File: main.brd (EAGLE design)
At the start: 49.5 x 51.7 mm, 37 parts, among them J1 CORTEX_DEBUG_PTH, U1 ATSAMD21G-A, U2 BNO055, U3 BQ24133_RGY_24

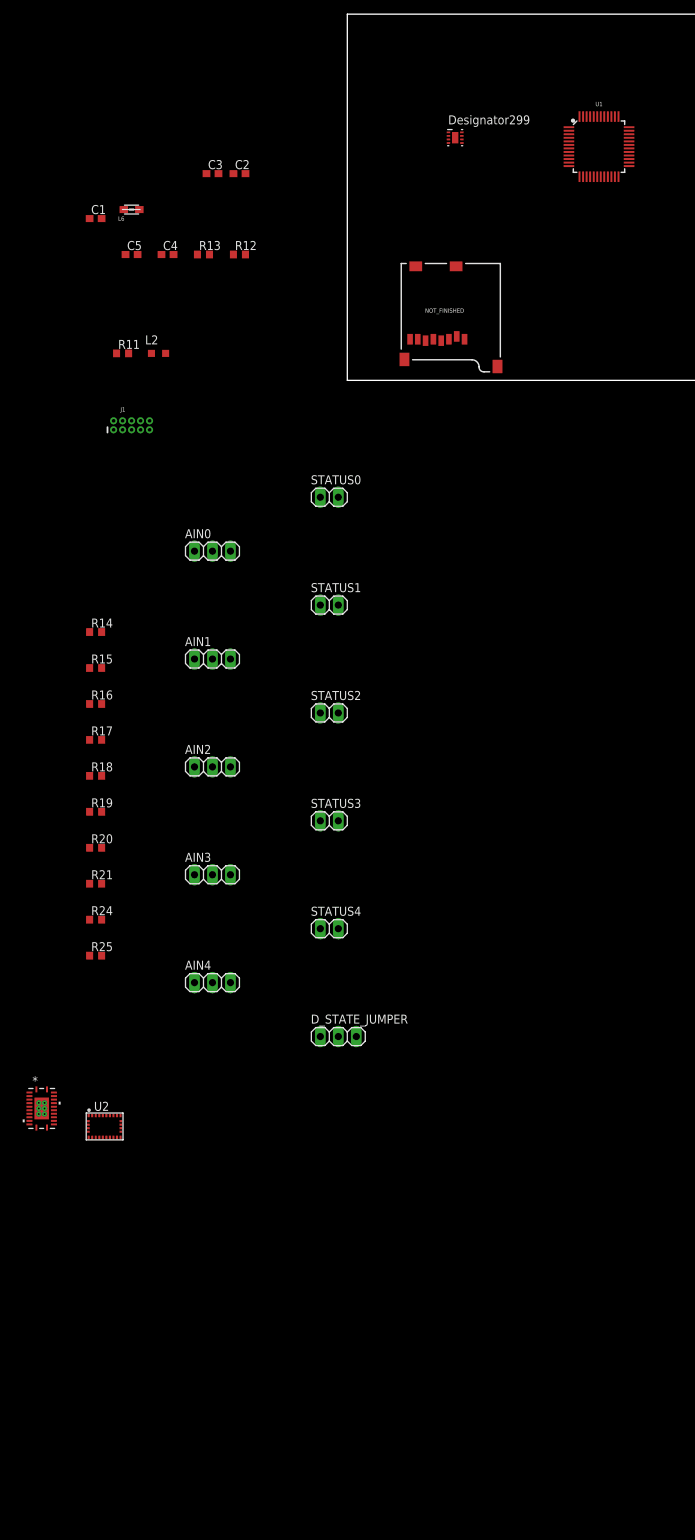
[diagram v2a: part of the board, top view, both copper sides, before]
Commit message: Added IMU Configuration
Added Imu Nets
Removed AIO and GPIO Net assignments for now, since they can go anywhere
Named SD CARD SPI pins accordingly, these should be final
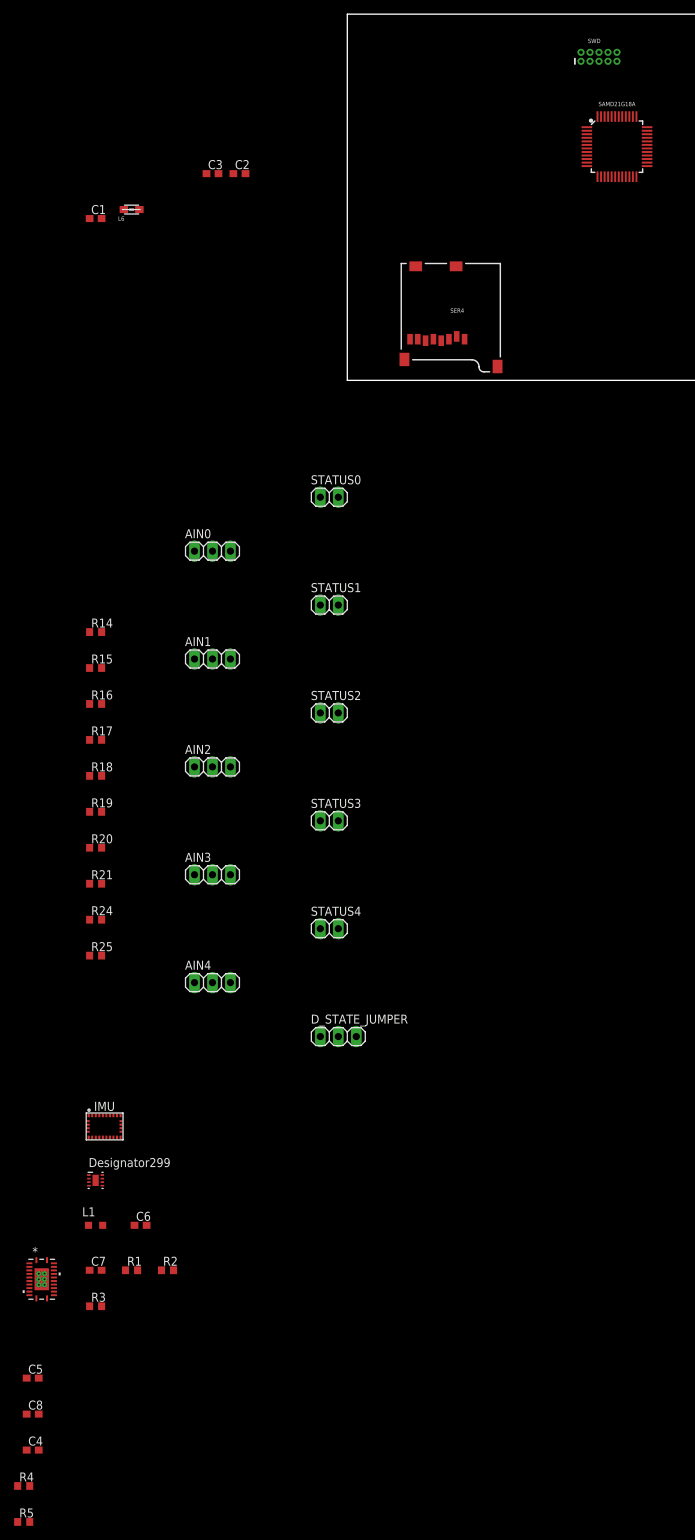
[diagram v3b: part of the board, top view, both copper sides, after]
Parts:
- removed J1: CORTEX_DEBUG_PTH, SparkFun-Connectors:2X5-PTH-1.27MM
- removed L2: REF, resistor:L2012C
- removed PWR_REG: (no value), TPS62162-Q1:DSG0008A
- removed R11, R12, R13: REF, resistor:R0603
- removed U1: ATSAMD21G-A, SparkFun-IC-Microcontroller:TQFP-48
- removed U3: BQ24133_RGY_24, BQ24133:RGY24_2P05X3P1
- added 3.3V_REG: (no value), TPS62162-Q1:DSG0008A
- added C6, C7: REF, resistor:C0603
- added C8: 100nF, resistor:C0603
- added L1: REF, resistor:L2012C
- added POWER_CONTROLLER: BQ24133_RGY_24, BQ24133:RGY24_2P05X3P1
- added R1, R2, R3: REF, resistor:R0603
- added R4, R5: 10k, resistor:R0603
- added SAMD21G18A: ATSAMD21G-A, SparkFun-IC-Microcontroller:TQFP-48
- added SWD: CORTEX_DEBUG_PTH, SparkFun-Connectors:2X5-PTH-1.27MM
- C3: value 0.1uF -> 100nF
- C4: value REF -> 6.8nF
- C5: value REF -> 100nF
- moved C4 170.0 mm to (-44.5, -151.1)
- moved C5 159.4 mm to (-44.5, -141.0)
- renumbered NOT_FINISHED to SER4, U2 to IMU
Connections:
- removed net GNDIO: IMU.25
- removed net N$6: L2.1, PWR_REG.7
- removed net PIN10: IMU.10
- removed net PIN15: IMU.15
- removed net PIN16: IMU.16
- removed net SPI_DEFAULT_SS: U1.27
- removed net SPI_MISO: SER4.DO, U1.28
- removed net SPI_MOSI: SER4.DI, U1.25
- removed net SPI_SCK: SER4.SCLK, U1.26
- removed net VDD: IMU.3
- removed net VDDIO: IMU.28
- removed net ~RESET: J1.10, U1.40
- removed net ~SD_CS: SER4.CS
- new net *I2C_ADDR_SEL: IMU.17
- new net *I2C_SCL: IMU.19
- new net *I2C_SDA: IMU.20
- new net *INT: IMU.14
- new net *NBL_IMU: IMU.4
- new net *XIN32: IMU.27
- new net *XOUT32: IMU.26
- new net N$10: 3.3V_REG.5, R1.1, R2.2
- new net N$7: 3.3V_REG.7, L1.1
- new net NRESET: IMU.11, R4.2, R5.2, SAMD21G18A.40, SWD.10
- new net PA14_PORT: SAMD21G18A.23, SER4.CD1, SER4.CD2
- new net PA15_PORT: SAMD21G18A.24, SER4.CS
- new net PB08D_SER4_P0: SAMD21G18A.7, SER4.DI
- new net PB09D_SER4_P1: SAMD21G18A.8, SER4.SCLK
- new net PB11D_SER4_P3: SAMD21G18A.20, SER4.DO
- net 3.3V: now also 3.3V_REG.6, C4.1, C6.1, IMU.28, IMU.3, L1.2, R1.2, R3.2, R4.1, R5.1, SAMD21G18A.44, SWD.1; no longer J1.1, L2.2, PWR_REG.6, R11.2, R12.2, U1.44
- net AVCC: now also POWER_CONTROLLER.4; no longer U3.4
- net BTST: now also POWER_CONTROLLER.21; no longer U3.21
- net EPAD: now also POWER_CONTROLLER.25; no longer U3.25
- net GND: now also 3.3V_REG.1, 3.3V_REG.4, 3.3V_REG.9, C6.2, C7.2, C8.2, IMU.10, IMU.15, IMU.16, IMU.18, IMU.25, IMU.5, IMU.6, R2.1, SAMD21G18A.18, SAMD21G18A.35, SAMD21G18A.42, SAMD21G18A.5, SWD.3, SWD.5, SWD.9; no longer J1.3, J1.5, J1.9, PWR_REG.1, PWR_REG.4, PWR_REG.9, R13.1, U1.18, U1.35, U1.42, U1.5
- net N$2: now also SAMD21G18A.6; no longer U1.6
- net N$9: now also C8.1, IMU.9; no longer PWR_REG.5, R12.1, R13.2
- net PA02_AIN0: no longer U1.3
- net PA04_AIN4: no longer U1.9
- net PA05_AIN5: no longer U1.10
- net PA30_SWCLK: now also SAMD21G18A.45, SWD.4; no longer J1.4, U1.45
- net PA31_SWDIO: now also SAMD21G18A.46, SWD.2; no longer J1.2, U1.46
- net PB08_AIN2: no longer U1.7
- net PB09_AIN3: no longer U1.8
- net PG: now also 3.3V_REG.8, R3.1; no longer PWR_REG.8, R11.1
- net PGND: now also POWER_CONTROLLER.23; no longer U3.23
- net PGND_2: now also POWER_CONTROLLER.22; no longer U3.22
- net PVCC: now also POWER_CONTROLLER.3; no longer U3.3
- net PVCC_2: now also POWER_CONTROLLER.2; no longer U3.2
- net REGN: now also POWER_CONTROLLER.20; no longer U3.20
- net SW: now also POWER_CONTROLLER.24; no longer U3.24
- net SW_2: now also POWER_CONTROLLER.1; no longer U3.1
- net VDDCORE: now also SAMD21G18A.43; no longer U1.43
- net VIN: now also 3.3V_REG.2, 3.3V_REG.3, C7.1; no longer C4.1, PWR_REG.2, PWR_REG.3
- net VREF: now also POWER_CONTROLLER.12; no longer U3.12

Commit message: Added lib folder, added charge controller schematic
Almost finished naming nets and component values.
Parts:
- removed STATUS0, STATUS1, STATUS2, STATUS3, STATUS4: (no value), pinhead:1X02
- added BATT, V0, V1, V2: (no value), pinhead:1X02
- added C11, C21, C23: 1u, resistor:C0603
- added C12: 2.2u, resistor:C0603
- added C13, C14, C16, C18, C22: 100n, resistor:C0603
- added C15, C19, C20: 10u, resistor:C0603
- added C17: 47n, resistor:C0603
- added C9: 100nF, resistor:C0603
- added D1: BAS70-05, diode:SOT23
- added L2: 3.3u, resistor:L2012C
- added LED1: (no value), adafruit:CHIPLED_0603
- added Q1, Q2: 5.8A/30V/35mΩ, SparkFun-DiscreteSemi:SOT23-3
- added Q3: 2.5A/30V/105mΩ, SparkFun-DiscreteSemi:SOT23-3
- added R10: 2, resistor:R0603
- added R11, R12: 4.02k, resistor:R0603
- added R13: 20m, resistor:R0603
- added R23, R33: 0, resistor:R0603
- added R26: 1k, resistor:R0603
- added R27: 10m, resistor:R0603
- added R28: 232k, resistor:R0603
- added R29, R35: 32.4k, resistor:R0603
- added R30: 5.23k, resistor:R0603
- added R31: 30.1k, resistor:R0603
- added R32: 1.5k, resistor:R0603
- added R34, R9: 100k, resistor:R0603
- added R7: 10, resistor:R0603
- added R8: 1M, resistor:R0603
- added RS-485: (no value), pinhead:1X04
- added R_THERM: 103AT, pinhead:1X02
- added S1: (no value), switch:M251
- added U2: SN65HVD32_D_8, SN65HVD32:D8
- moved R4 209.6 mm to (44.5, 33.0)
- moved C4 209.6 mm to (45.7, 38.1)
- moved R5 209.6 mm to (44.5, 27.9)
- moved C8 206.3 mm to (40.6, 41.9)
- moved C5 203.6 mm to (36.8, 45.7)
- moved C6 160.7 mm to (43.2, 24.1)
- moved C7 160.7 mm to (36.8, 17.8)
- moved L1 160.7 mm to (36.8, 24.1)
- moved R1 160.7 mm to (41.9, 17.8)
- moved R2 160.7 mm to (47.0, 17.8)
- moved R3 160.7 mm to (36.8, 12.7)
- moved POWER_CONTROLLER 154.9 mm to (35.6, 6.35)
- moved 3.3V_REG 154.7 mm to (40.6, 21.6)
- moved IMU 132.9 mm to (26.7, 12.7)
- moved D_STATE_JUMPER 58.6 mm to (-6.35, -34.3)
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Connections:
- removed net AVCC: POWER_CONTROLLER.4
- removed net BTST: POWER_CONTROLLER.21
- removed net EPAD: POWER_CONTROLLER.25
- removed net GPIO_IN_3: STATUS3.2
- removed net GPIO_IN_4: STATUS4.2
- removed net PGND: POWER_CONTROLLER.23
- removed net PGND_2: POWER_CONTROLLER.22
- removed net PVCC: POWER_CONTROLLER.3
- removed net PVCC_2: POWER_CONTROLLER.2
- removed net REGN: POWER_CONTROLLER.20
- removed net SW: POWER_CONTROLLER.24
- removed net SW_2: POWER_CONTROLLER.1
- removed net VREF: POWER_CONTROLLER.12
- new net MCU_RX: U2.3
- new net MCU_TX: U2.2
- new net N$11: RS-485.2, U2.7
- new net N$12: RS-485.3, U2.6
- new net N$13: RS-485.4, U2.5
- new net N$14: D1.3, R7.1
- new net N$15: C12.1, R10.1
- new net N$16: Q1.2, Q2.2, R11.1
- new net N$17: Q1.1, Q2.1, R12.2
- new net N$19: Q3.1, R26.2
- new net N$20: LED1.A, R32.2
- new net N$6: RS-485.1, U2.8
- new net PC_ACDRV: POWER_CONTROLLER.8, R12.1
- new net PC_ACN: C13.2, C14.1, R13.1, R23.2
- new net PC_ACP: C13.1, POWER_CONTROLLER.6, Q2.3, R13.2
- new net PC_ACSET: POWER_CONTROLLER.17, R34.2, R35.1
- new net PC_AVCC: C11.1, POWER_CONTROLLER.4, R7.2
- new net PC_BTST: C17.2, POWER_CONTROLLER.21
- new net PC_CAN: POWER_CONTROLLER.5
- new net PC_CELL: POWER_CONTROLLER.14, R33.2
- new net PC_CMSRC: POWER_CONTROLLER.7, R11.2
- new net PC_ISET: POWER_CONTROLLER.13, R28.1, R29.2
- new net PC_NBATDRV: POWER_CONTROLLER.19, R26.1
- new net PC_OVPSET: POWER_CONTROLLER.18, R8.1, R9.2
- new net PC_PVCC: C15.1, POWER_CONTROLLER.2, POWER_CONTROLLER.3, Q3.2, R23.1, S1.2
- new net PC_REGN: C23.1, POWER_CONTROLLER.20
- new net PC_SRN: BATT.1, C16.1, C19.1, C20.1, POWER_CONTROLLER.15, Q3.3, R27.1
- new net PC_SRP: C16.2, C18.1, L2.2, POWER_CONTROLLER.16, R27.2
- new net PC_STAT: LED1.C, POWER_CONTROLLER.9
- new net PC_SW: C17.1, L2.1, POWER_CONTROLLER.1, POWER_CONTROLLER.24
- new net PC_TS: POWER_CONTROLLER.10, R30.2, R31.1, R_THERM.1
- new net PC_TTC: C22.1, POWER_CONTROLLER.11
- new net PC_VREF: C21.1, POWER_CONTROLLER.12, R28.2, R30.1, R32.1, R33.1, R34.1
- new net VSYS: 3.3V_REG.2, 3.3V_REG.3, AIN0.1, AIN1.1, AIN2.1, AIN3.1, AIN4.1, C7.1, R4.1, S1.3
- new net V_BATT: D1.1
- net 3.3V: now also C9.1, U2.1; no longer R4.1
- net D_STATE: now also V0.1, V1.1, V2.1; no longer STATUS0.1, STATUS1.1, STATUS2.1, STATUS3.1, STATUS4.1
- net GND: now also BATT.2, C11.2, C12.2, C14.2, C15.2, C18.2, C19.2, C20.2, C21.2, C22.2, C23.2, C9.2, POWER_CONTROLLER.22, POWER_CONTROLLER.23, POWER_CONTROLLER.25, R29.1, R31.2, R35.2, R9.1, R_THERM.2, U2.4
- net GPIO_IN_0: now also V0.2; no longer STATUS0.2
- net GPIO_IN_1: now also V1.2; no longer STATUS1.2
- net GPIO_IN_2: now also V2.2; no longer STATUS2.2
- net VIN: now also D1.2, Q1.3, R10.2, R8.2; no longer 3.3V_REG.2, 3.3V_REG.3, AIN0.1, AIN1.1, AIN2.1, AIN3.1, AIN4.1, C7.1
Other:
- board size 49.5 x 51.7 mm -> 50.8 x 50.8 mm

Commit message: Added and removed some i/o
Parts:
- removed AIN0, AIN1, AIN2, AIN3, AIN4, D_STATE_JUMPER: (no value), pinhead:1X03
- removed V0, V1, V2: (no value), pinhead:1X02
- added 3.3V, PVCC: (no value), pinhead:1X02
- added AIN: (no value), pinhead:1X05
- added GPIO: (no value), pinhead:1X03
- moved R_THERM 304.2 mm to (33.7, 3.17)
- moved C22 269.6 mm to (19.1, -50.8)
- moved C23 269.6 mm to (19.1, -55.9)
- moved LED1 269.6 mm to (17.8, -20.3)
- moved R31 269.6 mm to (22.9, -10.2)
- moved R32 269.6 mm to (22.9, -15.2)
- moved R33 269.6 mm to (22.9, -20.3)
- moved R34 269.6 mm to (17.8, -40.6)
- moved R35 269.6 mm to (17.8, -45.7)
- moved BATT 249.6 mm to (16.5, 3.17)
- moved C21 234.7 mm to (3.81, -30.5)
- moved R28 234.7 mm to (2.54, -20.3)
- moved R29 234.7 mm to (2.54, -25.4)
- moved R30 234.7 mm to (2.54, -35.6)
- moved S1 230.5 mm to (26.7, 45.7), flipped to the bottom
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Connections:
- net PA02_AIN0 renamed AIN0
- net PA04_AIN4 renamed AIN1
- net PA05_AIN5 renamed AIN2
- net PB08_AIN2 renamed AIN3
- net PB09_AIN3 renamed AIN4
- removed net D_STATE: D_STATE_JUMPER.2, V0.1, V1.1, V2.1
- removed net GPIO_IN_0: V0.2
- removed net GPIO_IN_1: V1.2
- removed net GPIO_IN_2: V2.2
- new net GPIO1: GPIO.1
- new net GPIO2: GPIO.2
- new net GPIO3: GPIO.3
- net 3.3V: now also 3.3V.1, R4.1; no longer D_STATE_JUMPER.1
- net GND: now also 3.3V.2, PVCC.2; no longer AIN0.2, AIN1.2, AIN2.2, AIN3.2, AIN4.2, D_STATE_JUMPER.3
- net N$1: now also AIN.2; no longer AIN1.3
- net N$3: now also AIN.3; no longer AIN2.3
- net N$4: now also AIN.4; no longer AIN3.3
- net N$5: now also AIN.5; no longer AIN4.3
- net N$8: now also AIN.1; no longer AIN0.3
- net VSYS: now also PVCC.1; no longer AIN0.1, AIN1.1, AIN2.1, AIN3.1, AIN4.1, R4.1
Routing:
- added copper zone on layer 16, net GND
- added copper zone on layer 1, net N$18

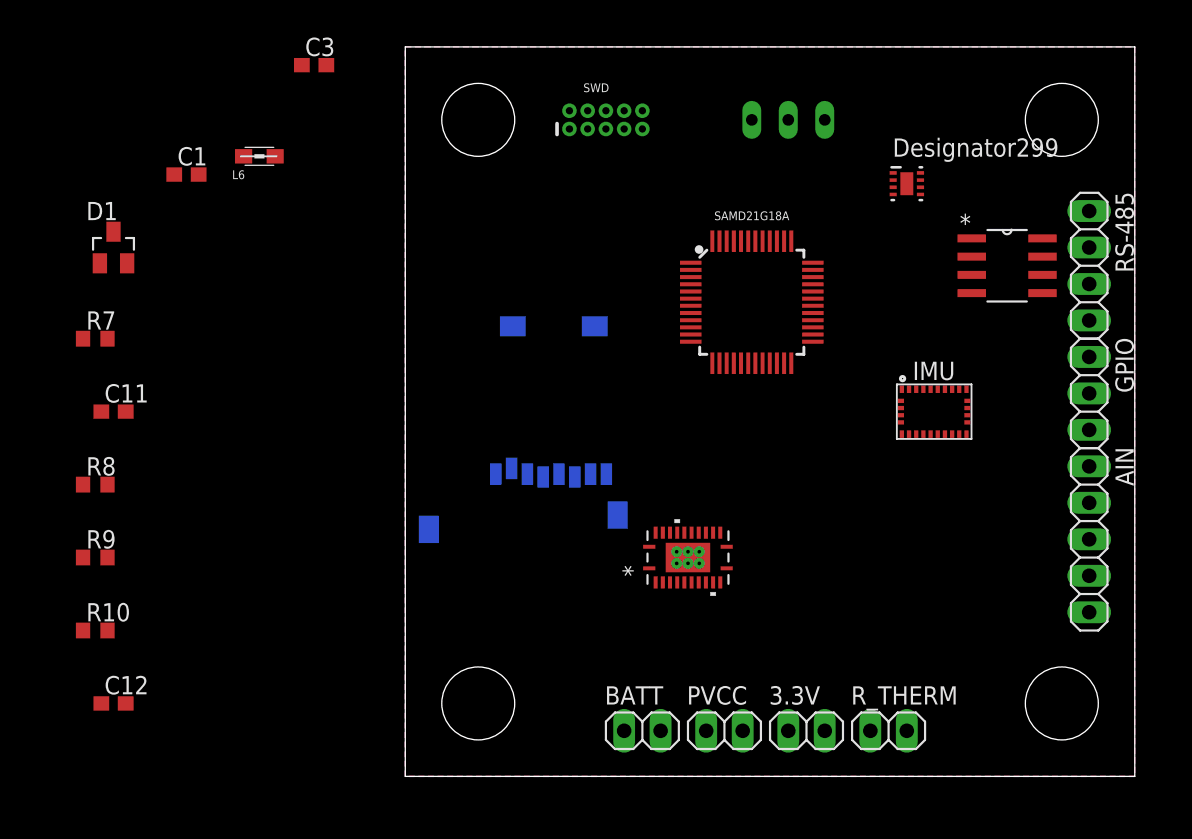
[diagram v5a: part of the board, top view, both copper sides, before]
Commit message: Started board design
Still need to add I2C, GPIO, and AIO nets in schematic. Need to also add status leds.
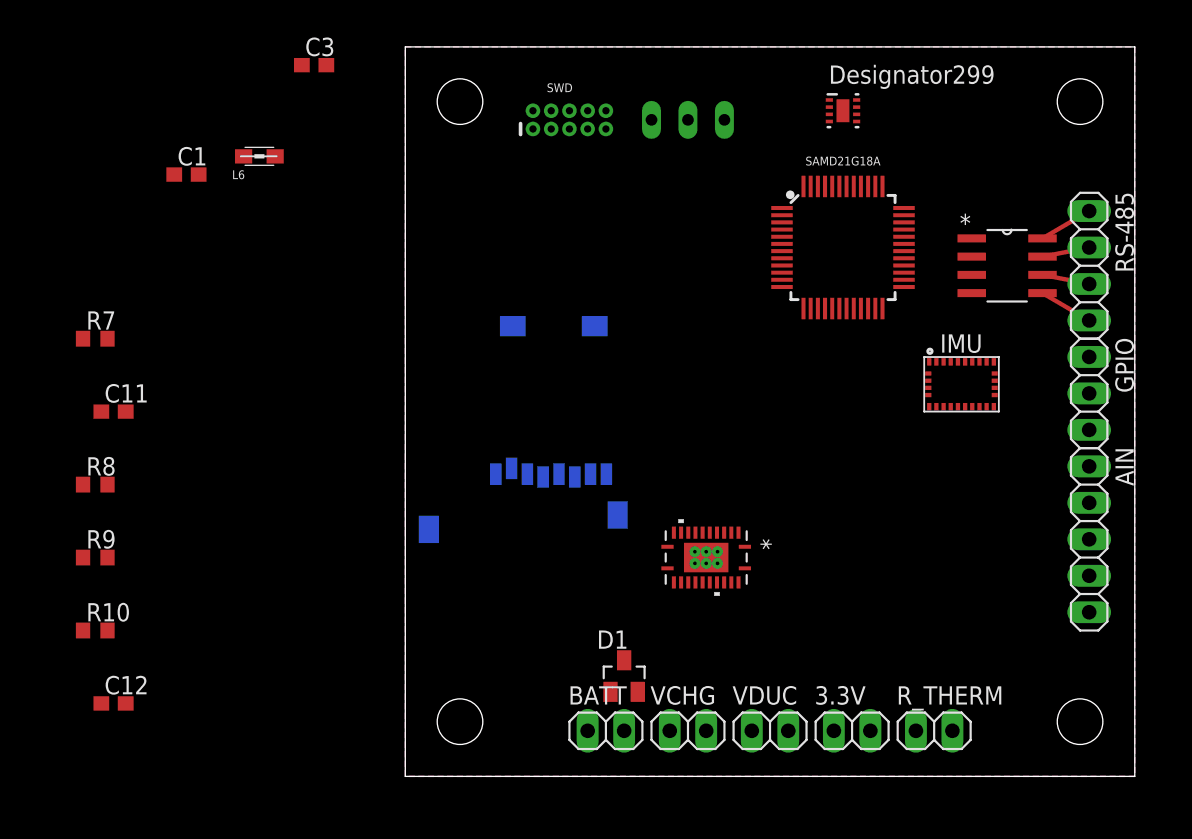
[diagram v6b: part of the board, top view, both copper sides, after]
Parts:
- removed PVCC: (no value), pinhead:1X02
- added U$1, U$2, U$3, U$4: (no value), special-drill:DRILL_0.1250
- added VCHG, VDUC: (no value), pinhead:1X02
- moved D1 46.4 mm to (15.2, 6.99)
- moved SAMD21G18A 7.41 mm to (30.5, 36.8)
- moved S1 6.99 mm to (19.7, 45.7)
- moved 3.3V_REG 6.75 mm to (30.5, 46.4)
- moved 3.3V 3.17 mm to (31.1, 3.17)
- moved R_THERM 3.17 mm to (36.8, 3.17)
- moved IMU 2.69 mm to (38.7, 27.3)
- moved BATT 2.54 mm to (14.0, 3.17)
- moved SWD 2.54 mm to (11.4, 45.7)
- moved POWER_CONTROLLER 1.27 mm to (21.0, 15.2), turned to 270 degrees
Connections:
- net GND: now also VCHG.2, VDUC.2; no longer PVCC.2
- net MCU_RX: now also SAMD21G18A.38
- net MCU_TX: now also SAMD21G18A.37
- net VIN: now also VCHG.1
- net VSYS: now also VDUC.1; no longer PVCC.1
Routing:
- net N$13: track 0.00 -> 3.77 mm
- net N$6: track 0.00 -> 3.77 mm
- net N$12: track 0.00 -> 3.31 mm
- net N$11: track 0.00 -> 3.31 mm
- added copper zone on layer 1, net GND
- removed copper zone on layer 1, net N$18
